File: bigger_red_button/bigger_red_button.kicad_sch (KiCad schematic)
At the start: 18 parts, among them J1 Conn_02x05_Odd_Even, J2 USB_C_Receptacle_USB2.0_16P, J3 Conn_02x01, J4 Conn_02x01, Q1 AO3400A, U1 USBLC6-2SC6, U2 TPS7A0533PDBV, U3 STM32G0B1KBTx

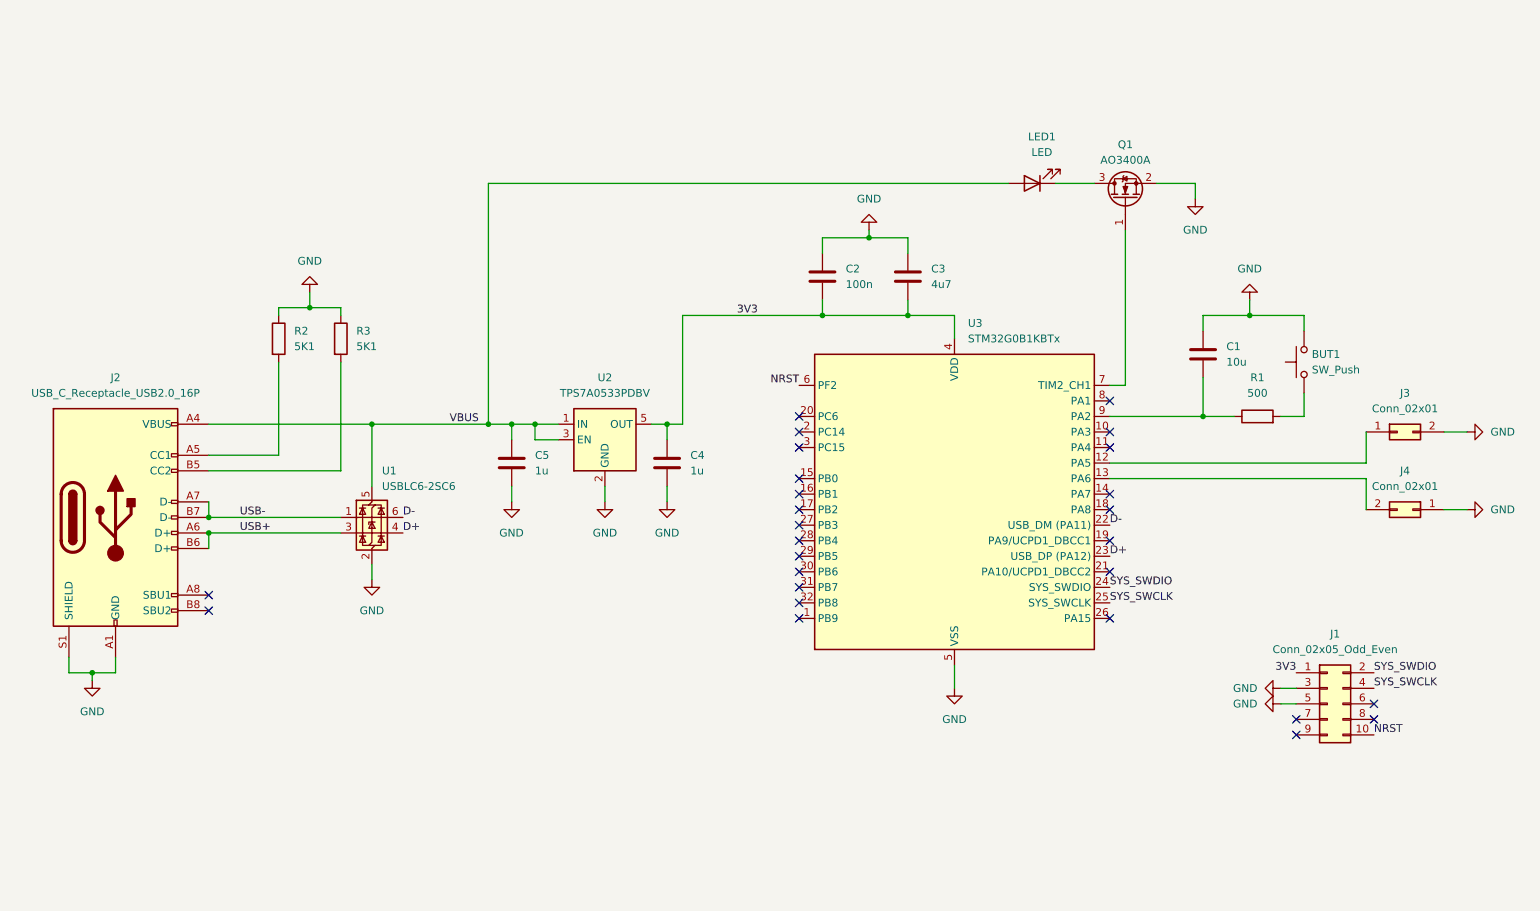
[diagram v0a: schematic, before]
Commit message: Use high-power LED driver instead of FET
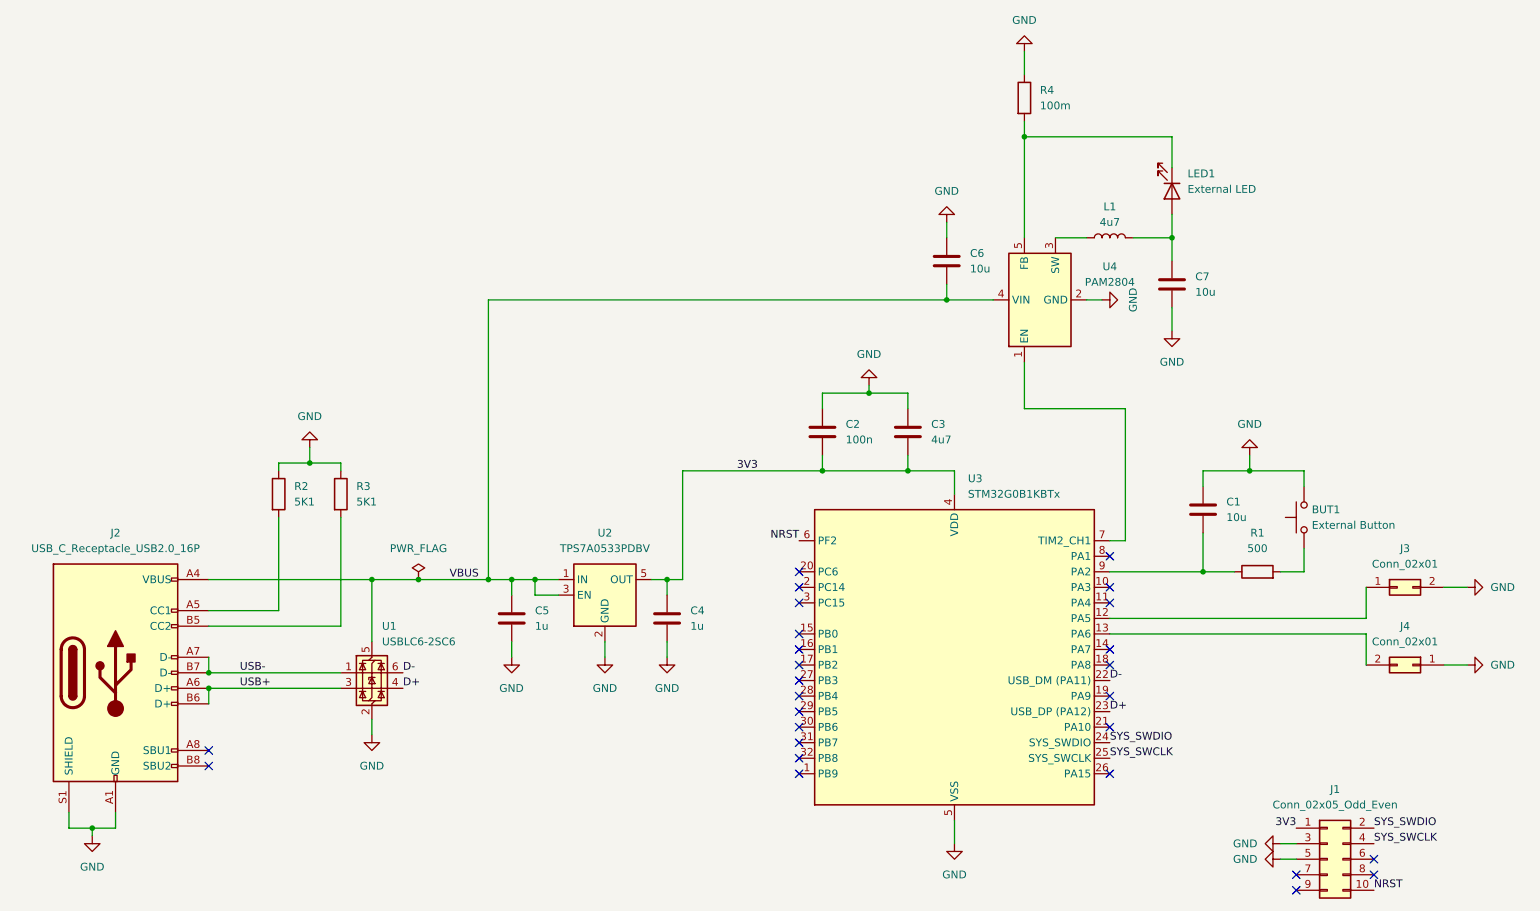
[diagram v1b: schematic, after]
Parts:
- removed Q1: AO3400A, Package_TO_SOT_SMD:SOT-23, symbol Transistor_FET:AO3400A
- added C6, C7: 10u, Capacitor_SMD:C_0402_1005Metric, symbol Device:C
- added L1: 4u7, Inductor_SMD:L_1008_2520Metric, symbol Device:L
- added R4: 100m, Resistor_SMD:R_1206_3216Metric, symbol Device:R
- added U4: PAM2804, Package_TO_SOT_SMD:TSOT-23-5, symbol Project_Components:PAM2804
- BUT1: value SW_Push -> External Button
- LED1: value LED -> External LED
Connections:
- net GND: now also C6.1, C7.2, R4.1, U4.2 (GND)
- net VBUS: now also C6.2, U4.4 (VIN); no longer LED1.2 (A)
- net at U3.7 (PA0): now also U4.1 (EN)
- net at LED1.1 (K): now also R4.2, U4.5 (FB)
- new net: C7.1, L1.2, LED1.2 (A)
- new net: L1.1, U4.3 (SW)
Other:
- moved on the sheet: BUT1, C1, C2, C3, C4, C5, J1, J2, J3, J4, LED1, R1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

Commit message: Replace G0 MCU with C0
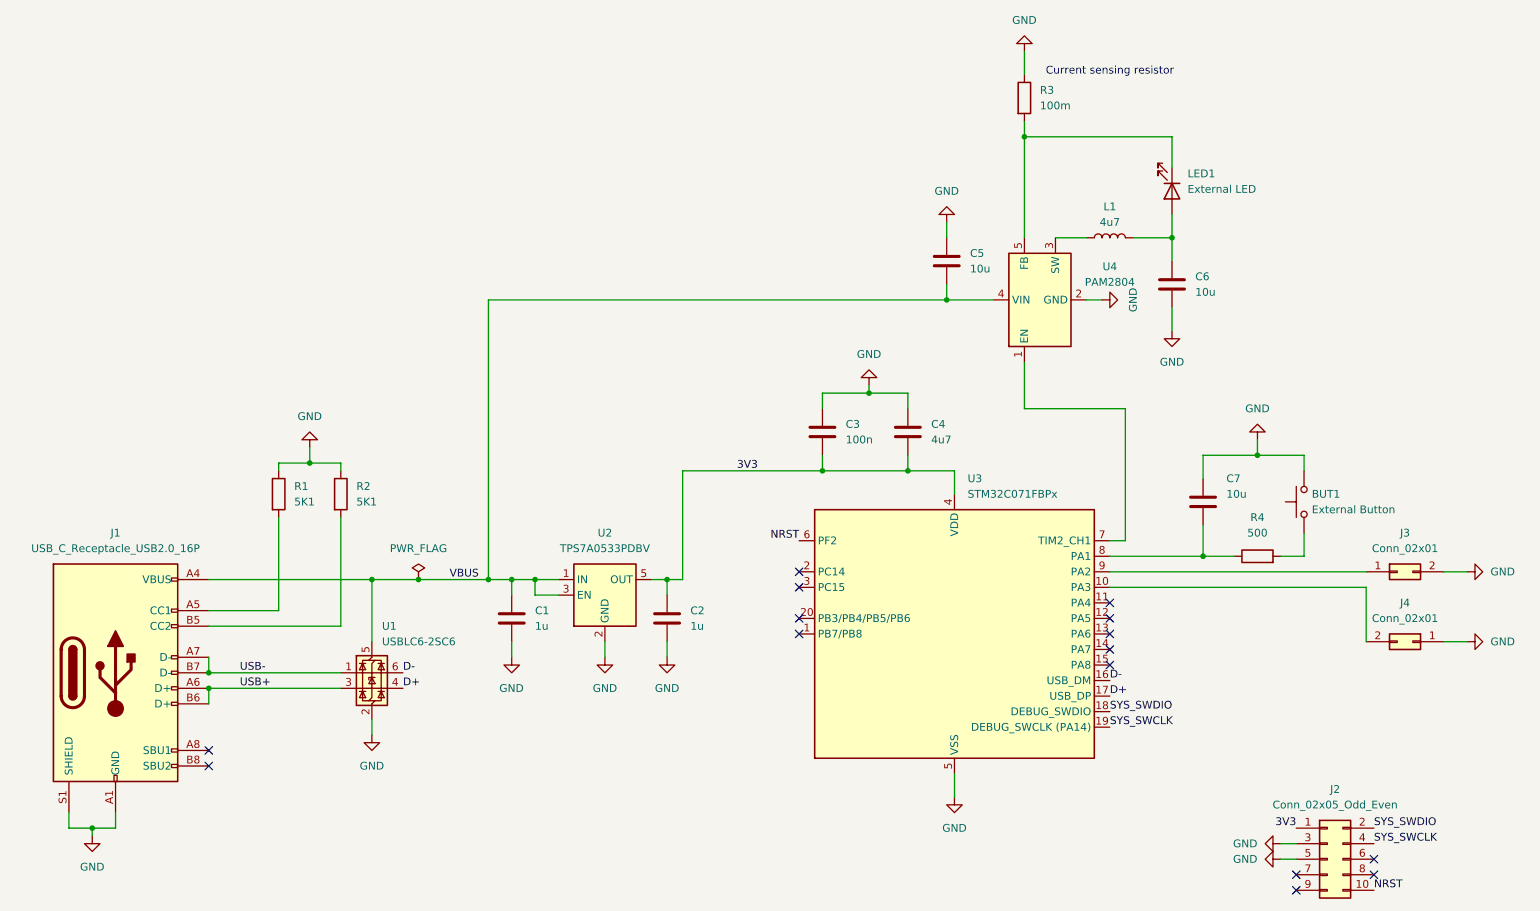
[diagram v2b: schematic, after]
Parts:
- removed U3: STM32G0B1KBTx, Package_QFP:LQFP-32_7x7mm_P0.8mm, symbol MCU_ST_STM32G0:STM32G0B1KBTx
- added U3: STM32C071FBPx, Package_SO:TSSOP-20_4.4x6.5mm_P0.65mm, symbol MCU_ST_STM32C0:STM32C071FBPx
- renumbered C5 to C1, C4 to C2, C2 to C3, C3 to C4, C6 to C5, C7 to C6, C1 to C7, J2 to J1, J1 to J2, R2 to R1, R3 to R2, R4 to R3, R1 to R4
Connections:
- net 3V3: now also U3.4 (VDD)
- net D+: now also U3.17 (PA12)
- net D-: now also U3.16 (PA11)
- net GND: now also U3.5 (VSS)
- net NRST: now also U3.6 (PF2)
- net SYS_SWCLK: now also U3.19 (PA14/PA15)
- net SYS_SWDIO: now also U3.18 (PA13)
- net at J3.1 (Pin_1): now also U3.9 (PA2)
- net at J4.2 (Pin_2): now also U3.10 (PA3)
- net at U4.1 (EN): now also U3.7 (PA0)
- net at C7.2, R4.1: now also U3.8 (PA1)
- no-connect marks 27 -> 15
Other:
- note added: "Current sensing resistor"
- moved on the sheet: BUT1, C7, J3, J4, R4

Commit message: Replace jumper symbols
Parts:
- removed J3, J4: Conn_02x01, Connector_PinHeader_2.54mm:PinHeader_1x02_P2.54mm_Vertical, symbol Connector_Generic:Conn_02x01
- added JP1, JP2: Jumper_2_Open, Connector_PinHeader_2.54mm:PinHeader_1x02_P2.54mm_Vertical, symbol Jumper:Jumper_2_Open
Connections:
- net GND: now also JP1.2 (B), JP2.2 (B)
- net at U3.10 (PA3): now also JP2.1 (A)
- net at U3.9 (PA2): now also JP1.1 (A)
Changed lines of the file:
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@@
 	(wire
 		(pts
-			(xy 252.73 106.68) (xy 256.54 106.68)
+			(xy 254 106.68) (xy 257.81 106.68)
 		)
 		(stroke
@@
 	(wire
 		(pts
+			(xy 240.03 118.11) (xy 243.84 118.11)
+		)
+		(stroke
+			(width 0)
+			(type default)
+		)
+	)
+	(wire
+		(pts
 			(xy 213.36 99.06) (xy 213.36 104.14)
 		)
@@
 	(wire
 		(pts
-			(xy 198.12 106.68) (xy 240.03 106.68)
+			(xy 198.12 106.68) (xy 243.84 106.68)
 		)
 		(stroke
@@
 	(wire
 		(pts
-			(xy 252.73 118.11) (xy 256.54 118.11)
+			(xy 254 118.11) (xy 257.81 118.11)
 		)
 		(stroke
@@
 	)
 	(symbol
+		(lib_id "Jumper:Jumper_2_Open")
+		(at 248.92 106.68 0)
+		(unit 1)
+		(exclude_from_sim no)
+		(in_bom yes)
+		(on_board yes)
+		(dnp no)
+		(fields_autoplaced yes)
+		(property "Reference" "JP1"
+			(at 248.92 100.33 0)
+			(effects
+				(font
+					(size 1.27 1.27)
+				)
+			)
+		)
+		(property "Value" "Jumper_2_Open"
+			(at 248.92 102.87 0)
+			(effects
+				(font
+					(size 1.27 1.27)
+				)
+			)
+		)
+		(property "Footprint" "Connector_PinHeader_2.54mm:PinHeader_1x02_P2.54mm_Vertical"
+			(at 248.92 106.68 0)
+			(effects
+				(font
+					(size 1.27 1.27)
+				)
+				(hide yes)
+			)
+		)
+		(property "Datasheet" "~"
+			(at 248.92 106.68 0)
+			(effects
+				(font
+					(size 1.27 1.27)
+				)
+				(hide yes)
+			)
+		)
+		(property "Description" "Jumper, 2-pole, open"
+			(at 248.92 106.68 0)
+			(effects
+				(font
+					(size 1.27 1.27)
+				)
+				(hide yes)
+			)
+		)
+		(pin "2"
+		)
+		(pin "1"
+		)
+		(instances
+			(project ""
+				(path "/feb3b749-4f34-4ca1-ab65-70106c7bdece"
+					(reference "JP1")
+					(unit 1)
+				)
+			)
+		)
+	)
+	(symbol
 		(lib_id "Device:C")
 		(at 100.33 114.3 0)
@@
 	(symbol
 		(lib_id "power:GND")
-		(at 256.54 118.11 90)
+		(at 257.81 118.11 90)
 		(unit 1)
 		(exclude_from_sim no)
@@
 		(fields_autoplaced yes)
 		(property "Reference" "#PWR017"
-			(at 262.89 118.11 0)
+			(at 264.16 118.11 0)
 			(effects
 				(font
@@
 		)
 		(property "Value" "GND"
-			(at 260.35 118.1099 90)
+			(at 261.62 118.1099 90)
 			(effects
 				(font
@@
 		)
 		(property "Footprint" ""
-			(at 256.54 118.11 0)
+			(at 257.81 118.11 0)
 			(effects
 				(font
@@
 		)
 		(property "Datasheet" ""
-			(at 256.54 118.11 0)
+			(at 257.81 118.11 0)
 			(effects
 				(font
@@
 		)
 		(property "Description" "Power symbol creates a global label with name \"GND\" , ground"
-			(at 256.54 118.11 0)
+			(at 257.81 118.11 0)
 			(effects
 				(font
@@
 	)
 	(symbol
-		(lib_id "Connector_Generic:Conn_02x01")
-		(at 245.11 106.68 0)
-		(unit 1)
-		(exclude_from_sim no)
-		(in_bom no)
-		(on_board yes)
-		(dnp no)
-		(fields_autoplaced yes)
-		(property "Reference" "J3"
-			(at 246.38 100.33 0)
-			(effects
-				(font
-					(size 1.27 1.27)
-				)
-			)
-		)
-		(property "Value" "Conn_02x01"
-			(at 246.38 102.87 0)
-			(effects
-				(font
-					(size 1.27 1.27)
-				)
-			)
-		)
-		(property "Footprint" "Connector_PinHeader_2.54mm:PinHeader_1x02_P2.54mm_Vertical"
-			(at 245.11 106.68 0)
-			(effects
-				(font
-					(size 1.27 1.27)
-				)
-				(hide yes)
-			)
-		)
-		(property "Datasheet" "~"
-			(at 245.11 106.68 0)
-			(effects
-				(font
-					(size 1.27 1.27)
-				)
-				(hide yes)
-			)
-		)
-		(property "Description" "Generic connector, double row, 02x01, this symbol is compatible with counter-clockwise, top-bottom and odd-even numbering schemes., script generated (kicad-library-utils/schlib/autogen/connector/)"
-			(at 245.11 106.68 0)
-			(effects
-				(font
-					(size 1.27 1.27)
-				)
-				(hide yes)
-			)
-		)
-		(pin "1"
-		)
-		(pin "2"
-		)
-		(instances
-			(project ""
-				(path "/feb3b749-4f34-4ca1-ab65-70106c7bdece"
-					(reference "J3")
-					(unit 1)
-				)
-			)
-		)
-	)
-	(symbol
 		(lib_id "Device:C")
 		(at 213.36 95.25 0)
@@
 	(symbol
 		(lib_id "power:GND")
-		(at 256.54 106.68 90)
+		(at 257.81 106.68 90)
 		(unit 1)
 		(exclude_from_sim no)
@@
 		(fields_autoplaced yes)
 		(property "Reference" "#PWR016"
-			(at 262.89 106.68 0)
+			(at 264.16 106.68 0)
 			(effects
 				(font
@@
 		)
 		(property "Value" "GND"
-			(at 260.35 106.6799 90)
+			(at 261.62 106.6799 90)
 			(effects
 				(font
@@
 		)
 		(property "Footprint" ""
-			(at 256.54 106.68 0)
+			(at 257.81 106.68 0)
 			(effects
 				(font
@@
 		)
 		(property "Datasheet" ""
-			(at 256.54 106.68 0)
+			(at 257.81 106.68 0)
 			(effects
 				(font
@@
 		)
 		(property "Description" "Power symbol creates a global label with name \"GND\" , ground"
-			(at 256.54 106.68 0)
+			(at 257.81 106.68 0)
 			(effects
 				(font
@@
 	)
 	(symbol
-		(lib_id "Connector_Generic:Conn_02x01")
-		(at 247.65 118.11 0)
-		(mirror y)
+		(lib_id "power:GND")
+		(at 125.73 120.65 0)
 		(unit 1)
 		(exclude_from_sim no)
-		(in_bom no)
+		(in_bom yes)
 		(on_board yes)
 		(dnp no)
-		(property "Reference" "J4"
-			(at 246.38 111.76 0)
+		(fields_autoplaced yes)
+		(property "Reference" "#PWR06"
+			(at 125.73 127 0)
 			(effects
 				(font
 					(size 1.27 1.27)
 				)
+				(hide yes)
 			)
 		)
-		(property "Value" "Conn_02x01"
-			(at 246.38 114.3 0)
+		(property "Value" "GND"
+			(at 125.73 125.73 0)
 			(effects
 				(font
@@
 			)
 		)
-		(property "Footprint" "Connector_PinHeader_2.54mm:PinHeader_1x02_P2.54mm_Vertical"
-			(at 247.65 118.11 0)
+		(property "Footprint" ""
+			(at 125.73 120.65 0)
 			(effects
 				(font
@@
 			)
 		)
-		(property "Datasheet" "~"
-			(at 247.65 118.11 0)
+		(property "Datasheet" ""
+			(at 125.73 120.65 0)
 			(effects
 				(font
@@
 			)
 		)
-		(property "Description" "Generic connector, double row, 02x01, this symbol is compatible with counter-clockwise, top-bottom and odd-even numbering schemes., script generated (kicad-library-utils/schlib/autogen/connector/)"
-			(at 247.65 118.11 0)
+		(property "Description" "Power symbol creates a global label with name \"GND\" , ground"
+			(at 125.73 120.65 0)
 			(effects
 				(font
@@
 			)
 		)
-		(pin "2"
-		)
 		(pin "1"
 		)
@@
 			(project ""
 				(path "/feb3b749-4f34-4ca1-ab65-70106c7bdece"
-					(reference "J4")
+					(reference "#PWR06")
 					(unit 1)
 				)
@@
 	)
 	(symbol
-		(lib_id "power:GND")
-		(at 125.73 120.65 0)
+		(lib_id "Jumper:Jumper_2_Open")
+		(at 248.92 118.11 0)
 		(unit 1)
 		(exclude_from_sim no)
@@
 		(dnp no)
 		(fields_autoplaced yes)
-		(property "Reference" "#PWR06"
-			(at 125.73 127 0)
+		(property "Reference" "JP2"
+			(at 248.92 111.76 0)
 			(effects
 				(font
 					(size 1.27 1.27)
 				)
-				(hide yes)
 			)
 		)
-		(property "Value" "GND"
-			(at 125.73 125.73 0)
+		(property "Value" "Jumper_2_Open"
+			(at 248.92 114.3 0)
 			(effects
 				(font
@@
 			)
 		)
-		(property "Footprint" ""
-			(at 125.73 120.65 0)
+		(property "Footprint" "Connector_PinHeader_2.54mm:PinHeader_1x02_P2.54mm_Vertical"
+			(at 248.92 118.11 0)
 			(effects
 				(font
@@
 			)
 		)
-		(property "Datasheet" ""
-			(at 125.73 120.65 0)
+		(property "Datasheet" "~"
+			(at 248.92 118.11 0)
 			(effects
 				(font
@@
 			)
 		)
-		(property "Description" "Power symbol creates a global label with name \"GND\" , ground"
-			(at 125.73 120.65 0)
+		(property "Description" "Jumper, 2-pole, open"
+			(at 248.92 118.11 0)
 			(effects
 				(font
@@
 		(pin "1"
 		)
+		(pin "2"
+		)
 		(instances
 			(project ""
 				(path "/feb3b749-4f34-4ca1-ab65-70106c7bdece"
-					(reference "#PWR06")
+					(reference "JP2")
 					(unit 1)
 				)

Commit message: Reroute PCB
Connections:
- net at JP1.1 (A): now also U3.8 (PA1); no longer U3.9 (PA2)
- net at C7.2, R4.1: now also U3.7 (PA0); no longer U3.8 (PA1)
- net at U3.10 (PA3): now also U4.1 (EN); no longer JP2.1 (A)
- new net: JP2.1 (A), U3.9 (PA2)
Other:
- moved on the sheet: BUT1, C7, JP1, JP2, R4
